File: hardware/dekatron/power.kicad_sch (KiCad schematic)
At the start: 114 parts, among them J101 PWR_IN, J102 NIX_12V, Q101 AOD4185, Q102 AOD5N40, U101 TPS54202, U102 LM66100, U103 LM66100, U104 LM66100, U105 LP2951 (adj. 10 V), U106 LM5156H, U107 TLV3011

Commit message: Tube sheet schematic; kit 15 uH buck inductor
tube.kicad_sch: G+/RTN zener regulator from V_B_BIAS (RTN 51 V sinks the
tube current and holds with zero tube current; G+ = 90 V), MMBTA42 guide
drivers, MMBTA92 index level shifter, 3 x 220k anode string, cathode
links LK6-LK14 and soldered harness landings. Net classes extended to
ANODE (HV) and the bias nets. BOM now covers both sheets (bom.csv).
Buck inductor from the user's kit: 15 uH, 1.31 A, 4 mm pitch.

Co-Authored-By: Claude Opus 5.5 <noreply@anthropic.com>
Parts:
- L101: footprint Inductor_SMD:L_Bourns_SRR1260 -> Inductor_THT:L_Radial_D6.0mm_P4.00mm; MPN SRR1260-150M -> (kit, 6 x 8 mm radial); Manufacturer Bourns -> (none); Rating Isat >= 2.5 A -> Rated 1.31 A; limits the 5 V rail to ~1.3 A
- L102: Rating Rated 0.71 A, DCR 0.35 ohm; confirm lead pitch -> Rated 0.71 A, DCR 0.35 ohm, 4 mm pitch
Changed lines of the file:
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@@
 	  (property "Reference" "L101" (at 398.78 50.34 90) (show_name no) (do_not_autoplace no) (effects (font (size 1.27 1.27))))
 	  (property "Value" "15uH" (at 398.78 57.34 90) (show_name no) (do_not_autoplace no) (effects (font (size 1.27 1.27))))
-	  (property "Footprint" "Inductor_SMD:L_Bourns_SRR1260" (at 398.78 53.34 90) (hide yes) (show_name no) (do_not_autoplace no) (effects (font (size 1.27 1.27)) (justify left)))
+	  (property "Footprint" "Inductor_THT:L_Radial_D6.0mm_P4.00mm" (at 398.78 53.34 90) (hide yes) (show_name no) (do_not_autoplace no) (effects (font (size 1.27 1.27)) (justify left)))
 	  (property "Datasheet" "" (at 398.78 53.34 90) (hide yes) (show_name no) (do_not_autoplace no) (effects (font (size 1.27 1.27)) (justify left)))
 	  (property "Description" "Inductor" (at 398.78 53.34 90) (hide yes) (show_name no) (do_not_autoplace no) (effects (font (size 1.27 1.27)) (justify left)))
 	  (property "Function" "Buck inductor" (at 398.78 53.34 90) (hide yes) (show_name no) (do_not_autoplace no) (effects (font (size 1.27 1.27)) (justify left)))
-	  (property "MPN" "SRR1260-150M" (at 398.78 53.34 90) (hide yes) (show_name no) (do_not_autoplace no) (effects (font (size 1.27 1.27)) (justify left)))
-	  (property "Manufacturer" "Bourns" (at 398.78 53.34 90) (hide yes) (show_name no) (do_not_autoplace no) (effects (font (size 1.27 1.27)) (justify left)))
-	  (property "Rating" "Isat >= 2.5 A" (at 398.78 53.34 90) (hide yes) (show_name no) (do_not_autoplace no) (effects (font (size 1.27 1.27)) (justify left)))
+	  (property "MPN" "(kit, 6 x 8 mm radial)" (at 398.78 53.34 90) (hide yes) (show_name no) (do_not_autoplace no) (effects (font (size 1.27 1.27)) (justify left)))
+	  (property "Rating" "Rated 1.31 A; limits the 5 V rail to ~1.3 A" (at 398.78 53.34 90) (hide yes) (show_name no) (do_not_autoplace no) (effects (font (size 1.27 1.27)) (justify left)))
 	  (pin "1")
 	  (pin "2")
@@
 	  (property "Function" "HV boost inductor" (at 340.36 170.18 90) (hide yes) (show_name no) (do_not_autoplace no) (effects (font (size 1.27 1.27)) (justify left)))
 	  (property "MPN" "(kit, 6 x 8 mm radial)" (at 340.36 170.18 90) (hide yes) (show_name no) (do_not_autoplace no) (effects (font (size 1.27 1.27)) (justify left)))
-	  (property "Rating" "Rated 0.71 A, DCR 0.35 ohm; confirm lead pitch" (at 340.36 170.18 90) (hide yes) (show_name no) (do_not_autoplace no) (effects (font (size 1.27 1.27)) (justify left)))
-	  (pin "1")
-	  (pin "2")
+	  (property "Rating" "Rated 0.71 A, DCR 0.35 ohm, 4 mm pitch" (at 340.36 170.18 90) (hide yes) (show_name no) (do_not_autoplace no) (effects (font (size 1.27 1.27)) (justify left)))
+	  (pin "1")
+	  (pin "2")

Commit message: Schematic review: add V_b overvoltage cutoff; fix bring-up step 2 and SW net class
Netlist checks (117 nets, 91 pin checks, GPIO map, net classes) pass.
Design review found V_b unprotected: with feedback and OVP on HV, an open
tripler part or link LK3 lets V_b run away. A second TLV3011 (2 x 1.0M /
12.4k, ~202 V) is wired-OR on EN/UVLO; simulated with an open tripler
diode, V_b holds at <= 199.3 V. Bring-up step 2 keeps the tripler
connected (LK4 open, HV dummy load); V_b dummy loads removed. Net-class
pattern *SW -> */SW so the buck switch node keeps default clearance.

Co-Authored-By: Claude Opus 5.5 <noreply@anthropic.com>
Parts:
- removed R144: 8.2k, Resistor_SMD:R_1206_3216Metric, symbol Device:R
- added C129: 1nF, Capacitor_SMD:C_1206_3216Metric, symbol Device:C
- added C130: 0.1uF, Capacitor_SMD:C_1206_3216Metric, symbol Device:C
- added U108: TLV3011, Package_TO_SOT_SMD:SOT-23-6, symbol dekatron:TLV3011
- LK3: Function D11 link L3: V_b to the tripler DC column (wire link, desol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 -> D11 link L3: V_b to the tripler DC column (fault isolation;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
- R141: value 8.2k -> 1.0M; Function V_b dummy load 1/4 (bring-up only) -> V_b OVP string 1/2 (<= 100 V per part); now fitted
- R142: value 8.2k -> 1.0M; Function V_b dummy load 2/4 (bring-up only) -> V_b OVP string 2/2; now fitted
- R143: value 8.2k -> 12.4k; Function V_b dummy load 3/4 (bring-up only) -> V_b OVP divider, lower (trip ~202 V); Rating (none) -> 1 %; now fitted
- R145: Function HV dummy load 1/6 (bring-up only) -> HV dummy load 1/6 (bring-up only, LK4 open)
- R146: Function HV dummy load 2/6 (bring-up only) -> HV dummy load 2/6 (bring-up only, LK4 open)
- R147: Function HV dummy load 3/6 (bring-up only) -> HV dummy load 3/6 (bring-up only, LK4 open)
- R148: Function HV dummy load 4/6 (bring-up only) -> HV dummy load 4/6 (bring-up only, LK4 open)
- R149: Function HV dummy load 5/6 (bring-up only) -> HV dummy load 5/6 (bring-up only, LK4 open)
- R150: Function HV dummy load 6/6 (bring-up only) -> HV dummy load 6/6 (bring-up only, LK4 open)
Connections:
- net STR_DV3 is gone; now on net GND: R143.2
- net +5V: now also C130.1, U108.6 (V+)
- net GND: now also C129.2, C130.2, U108.2 (V-)
- net HV_EN_PIN: now also U108.1 (OUT)
- net STR_DV1 renamed STR_VO1
- net STR_DV2 renamed VB_OVP_SENSE
- net VB_OVP_SENSE: now also C129.1, U108.4 (IN-)
- new net VB_OVP_REF: U108.3 (IN+), U108.5 (REF)
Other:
- note added: "HV MONITOR (HV_SENSE, GP28), INDEPENDENT OVP on HV (~548 V) and on V_b (~202 V): both pull EN/UVLO low"
- note removed: "HV MONITOR (HV_SENSE, GP28) and INDEPENDENT OVP (TLV3011, trips at ~548 V, pulls EN/UVLO low)"

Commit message: Tie the dekatron cathodes at the socket; add Phase 1C PCB tooling (WIP)
Cathodes K0, K2-K9 are joined at the socket and return on one RTN wire, as
in the AD01 reference: LK6-LK14 and J203 removed, tube harness is anode
(J201) + G1, G2, K1, RTN (J202, 4 pads). Netlist diff: only the nine
TUBE_Kn nets and the RTN link pins change. ERC 1 (intentional).

Also adds work-in-progress PCB tooling: gen_pcb.py (pcbnew placement,
outline, pours, rules), route_pcb.py (class-aware A* router adapted from
nanovolt-divider), pcb_io.py, and dekatron.kicad_dru with the corrected
HV pair rules (HV to HV/VB/HVSTR 1.5 mm, to bias/logic 3.0 mm). Harness
landings use plain wire pads with cable-tie anchors. The board itself is
not committed yet: placement is being reworked.

Co-Authored-By: Claude Opus 5.5 <noreply@anthropic.com>
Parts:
- J101, J102: footprint Connector_Wire:SolderWire-0.5sqmm_1x02_P4.8mm_D0.9mm_OD2.3mm_Relief -> Connector_Wire:SolderWire-0.5sqmm_1x02_P4.8mm_D0.9mm_OD2.3mm
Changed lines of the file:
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@@
 	  (property "Reference" "J101" (at 33.68 44.72 0) (show_name no) (do_not_autoplace no) (effects (font (size 1.27 1.27)) (justify left)))
 	  (property "Value" "PWR_IN" (at 33.68 47.32 0) (show_name no) (do_not_autoplace no) (effects (font (size 1.27 1.27)) (justify left)))
-	  (property "Footprint" "Connector_Wire:SolderWire-0.5sqmm_1x02_P4.8mm_D0.9mm_OD2.3mm_Relief" (at 30.48 45.72 0) (hide yes) (show_name no) (do_not_autoplace no) (effects (font (size 1.27 1.27)) (justify left)))
+	  (property "Footprint" "Connector_Wire:SolderWire-0.5sqmm_1x02_P4.8mm_D0.9mm_OD2.3mm" (at 30.48 45.72 0) (hide yes) (show_name no) (do_not_autoplace no) (effects (font (size 1.27 1.27)) (justify left)))
 	  (property "Datasheet" "" (at 30.48 45.72 0) (hide yes) (show_name no) (do_not_autoplace no) (effects (font (size 1.27 1.27)) (justify left)))
 	  (property "Description" "Generic connector, single row, 01x02, script generated (kicad-library-utils/schlib/autogen/connector/)" (at 30.48 45.72 0) (hide yes) (show_name no) (do_not_autoplace no) (effects (font (size 1.27 1.27)) (justify left)))
@@
 	  (property "Reference" "J102" (at 285.14 44.72 0) (show_name no) (do_not_autoplace no) (effects (font (size 1.27 1.27)) (justify left)))
 	  (property "Value" "NIX_12V" (at 285.14 47.32 0) (show_name no) (do_not_autoplace no) (effects (font (size 1.27 1.27)) (justify left)))
-	  (property "Footprint" "Connector_Wire:SolderWire-0.5sqmm_1x02_P4.8mm_D0.9mm_OD2.3mm_Relief" (at 281.94 45.72 0) (hide yes) (show_name no) (do_not_autoplace no) (effects (font (size 1.27 1.27)) (justify left)))
+	  (property "Footprint" "Connector_Wire:SolderWire-0.5sqmm_1x02_P4.8mm_D0.9mm_OD2.3mm" (at 281.94 45.72 0) (hide yes) (show_name no) (do_not_autoplace no) (effects (font (size 1.27 1.27)) (justify left)))
 	  (property "Datasheet" "" (at 281.94 45.72 0) (hide yes) (show_name no) (do_not_autoplace no) (effects (font (size 1.27 1.27)) (justify left)))
 	  (property "Description" "Generic connector, single row, 01x02, script generated (kicad-library-utils/schlib/autogen/connector/)" (at 281.94 45.72 0) (hide yes) (show_name no) (do_not_autoplace no) (effects (font (size 1.27 1.27)) (justify left)))

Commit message: Redraw the dekatron schematics as wired, readable sheets
Each block is now drawn with real wires, power/GND symbols and junctions
instead of per-pin label stubs. Net names used by the PCB scripts and net
classes are kept as local labels; inter-sheet nets stay global labels.
Netlist pin partition verified identical to the previous version; ERC
unchanged (1 intentional LP2951/LM5156 power-output violation).

Co-Authored-By: Claude Opus 5.5 <noreply@anthropic.com>
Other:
- note added: "10 V GATE DRIVE"
- note added: "12 V INPUT (D4)"
- note added: "5 V BUCK"
- note added: "Bleeder, feedback, monitor and OVP strings, each part <= 150 V; always connected"
- note added: "Every capacitor and diode sees <= V_b; 47 ohm pump surge resistor; LK3 isolates the DC column for fault finding (never powered open)"
- note added: "Fuse, reverse-polarity P-MOSFET (gate clamped by D101), TVS, bulk; fused branch to the Nixie module"
- note added: "HV BOOST (D2, Phase 1B)"
- note added: "HV STRINGS (D2, D3, D12)"
- note added: "IDEAL DIODES (D6)"
- note added: "LM5156H, ~150 kHz DCM, 10 V gate drive, feedback from HV (tripler sheet area), CS filter against the pump surge; kit 100 uH inductor"
- note added: "LP2951 feeds LM5156 BIAS = VCC (2.97-16 V mode); 143k / 20.0k -> 10.07 V"
- note added: "One LM66100 per external 5 V feed; CE grounded = always on"
- note added: "TPS54202, TI reference design (SLVSD26C Fig. 7-1); 100k / 13.7k -> 4.95 V; UVLO 511k / 105k"
- note added: "TRIPLER (series-stack Cockcroft-Walton)"
- note removed: "10 V GATE DRIVE: LP2951 feeds LM5156 BIAS = VCC (2.97-16 V mode); 143k/20.0k -> 10.07 V"
- note removed: "12 V INPUT (D4): fuse, reverse-polarity P-MOSFET, TVS, bulk; Nixie module branch"
- note removed: "5 V BUCK: TPS54202, TI reference design (SLVSD26C Fig. 7-1); 100k/13.7k -> 4.95 V"
- note removed: "HV BOOST (D2, Phase 1B): LM5156H, ~150 kHz DCM, feedback from HV, CS filter, 10 V drive; kit 100 uH inductor"
- note removed: "HV MONITOR (HV_SENSE, GP28), INDEPENDENT OVP on HV (~548 V) and on V_b (~202 V): both pull EN/UVLO low"
- note removed: "IDEAL DIODES (D6): one LM66100 per external 5 V feed; CE grounded = always on"
- note removed: "TRIPLER (series-stack CW): every capacitor and diode sees <= V_b; 47 ohm pump surge resistor"
- moved on the sheet: F101, R134, R135

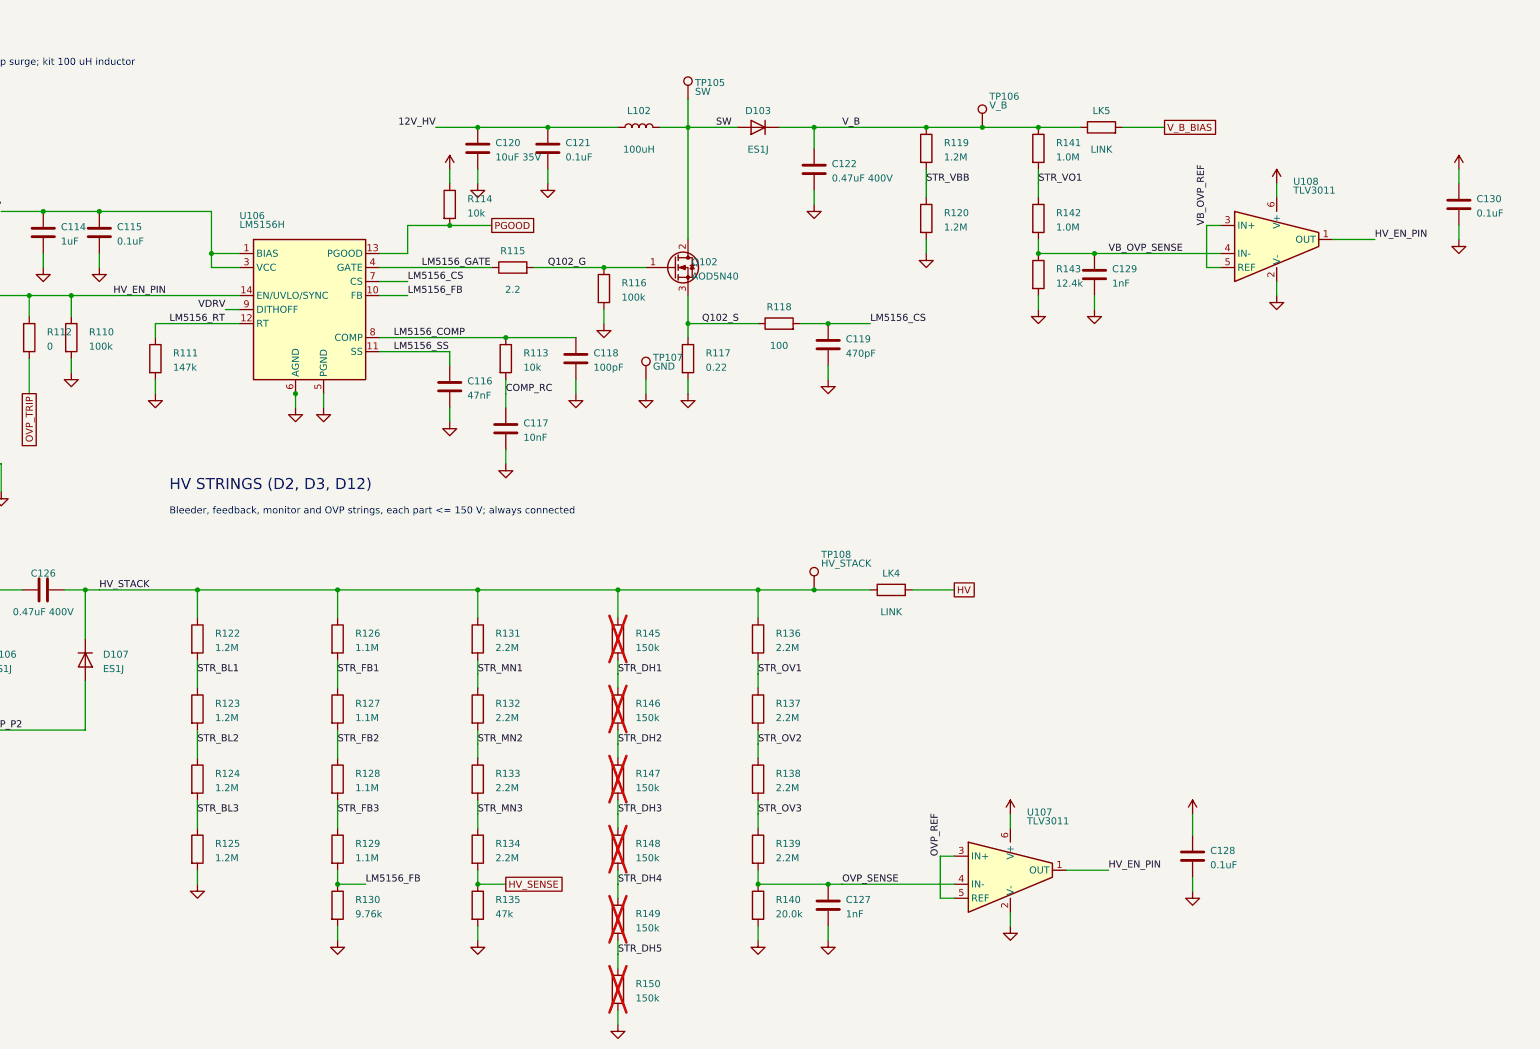
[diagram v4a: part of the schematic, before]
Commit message: Replace 1206 HV resistor strings with single leaded HVR25/HVR37 parts
- Drop the dedicated HV bleeder; the feedback divider (HVR25 4.75M/10.5k,
  453.4 V) and a shared monitor/OVP divider (HVR25 4.64M/14.0k/10.5k,
  OVP 551.8 V, HV_SENSE = HV/190.4) discharge HV: <50 V in 1.94 s,
  3.9 s with one divider open (hv_discharge.cir).
- Dummy load: one DNP HVR37 910k. V_b bleeder/OVP, RTN_SENSE, index
  divider: single HVR25. Anode: 2 x HVR37 332k. G+/RTN feed: MRS25 40.2k.
- C304 (HV_SENSE) 100 nF -> 10 nF: on a feedback-open runaway the shared
  OVP tap lagged HV by 15.8 V with 100 nF (fault_fbopen.cir).
- BOM 180 -> 155 parts; ERC unchanged.

Co-Authored-By: Claude Opus 5.5 <noreply@anthropic.com>
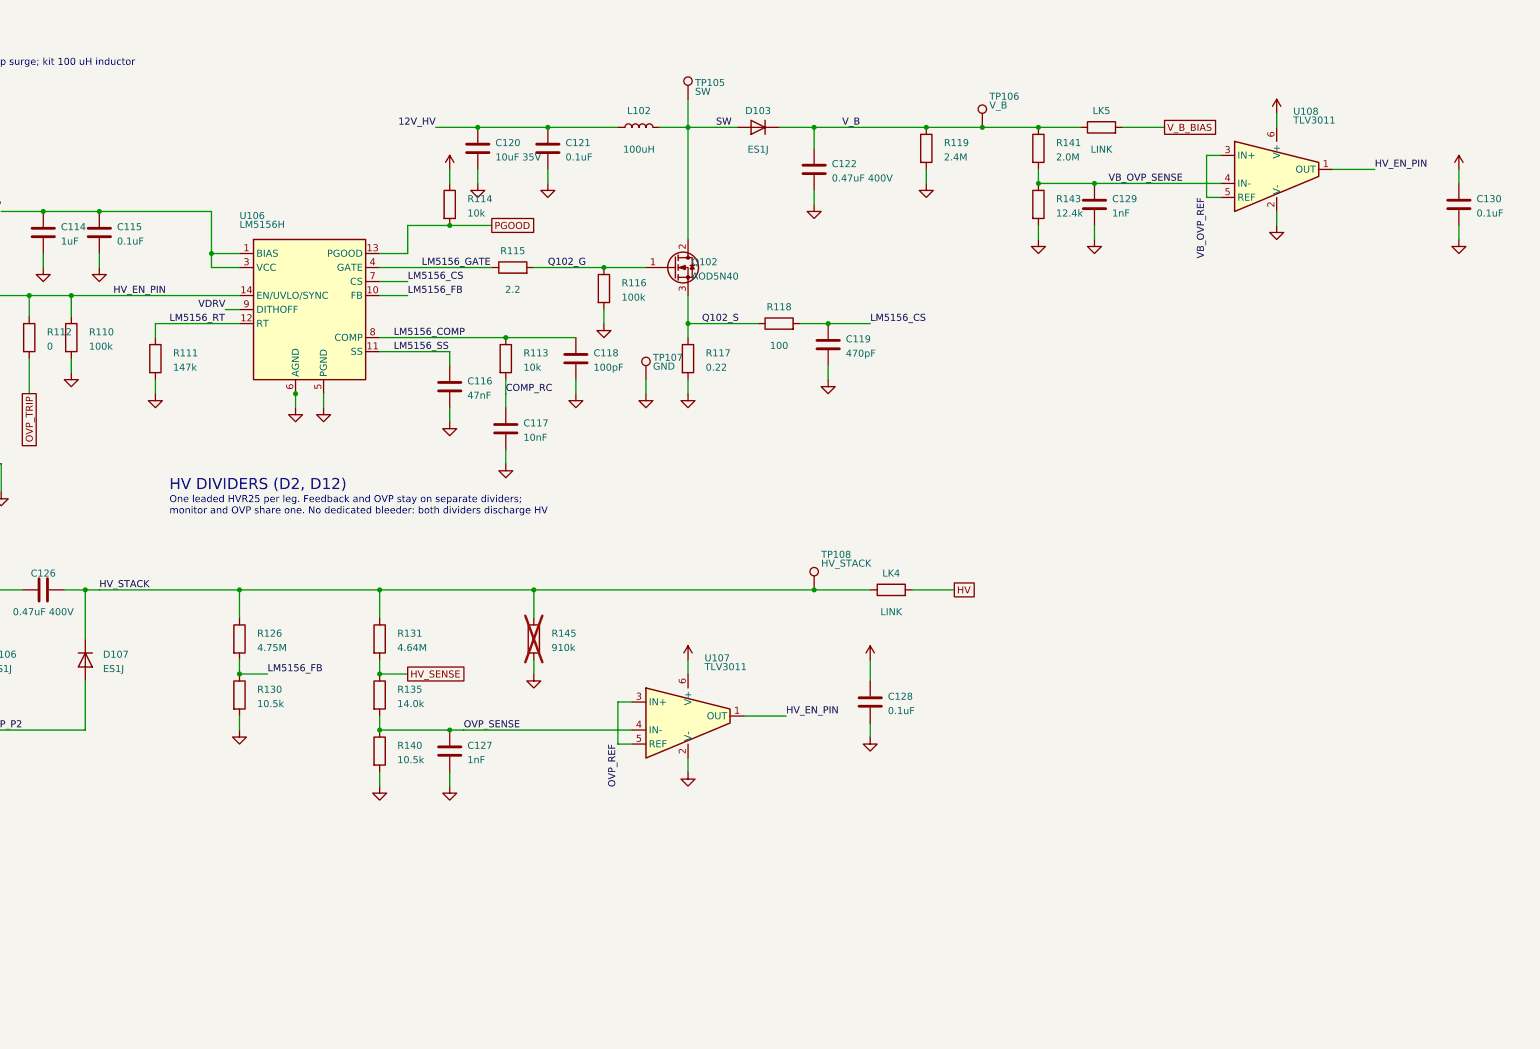
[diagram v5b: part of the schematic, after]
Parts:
- removed R120, R122, R123, R124, R125: 1.2M, Resistor_SMD:R_1206_3216Metric, symbol Device:R
- removed R127, R128, R129: 1.1M, Resistor_SMD:R_1206_3216Metric, symbol Device:R
- removed R132, R133, R134, R136, R137, R138, R139: 2.2M, Resistor_SMD:R_1206_3216Metric, symbol Device:R
- removed R142: 1.0M, Resistor_SMD:R_1206_3216Metric, symbol Device:R
- removed R146, R147, R148, R149, R150: 150k, Resistor_SMD:R_1206_3216Metric, symbol Device:R
- R119: value 1.2M -> 2.4M; footprint Resistor_SMD:R_1206_3216Metric -> Resistor_THT:R_Axial_DIN0207_L6.3mm_D2.5mm_P10.16mm_Horizontal; Function V_b bleeder 1/2 -> V_b bleeder (V_b's own discharge path with L3 open); MPN (none) -> HVR2500002404FR500; Manufacturer (none) -> Vishay; Rating (none) -> HVR25: 0.25 W, 1600 V DC, 1 %, 200 ppm/K
- R126: value 1.1M -> 4.75M; footprint Resistor_SMD:R_1206_3216Metric -> Resistor_THT:R_Axial_DIN0207_L6.3mm_D2.5mm_P10.16mm_Horizontal; Function HV feedback string 1/4 -> HV feedback divider, upper; MPN (none) -> HVR2500004754FR500; Manufacturer (none) -> Vishay; Rating (none) -> HVR25: 0.25 W, 1600 V DC, 1 %, 200 ppm/K
- R130: value 9.76k -> 10.5k; Function HV feedback, lower (451.8 V; 8.87k for 500 V) -> HV feedback, lower (453.4 V; 9.53k for 500 V)
- R131: value 2.2M -> 4.64M; footprint Resistor_SMD:R_1206_3216Metric -> Resistor_THT:R_Axial_DIN0207_L6.3mm_D2.5mm_P10.16mm_Horizontal; Function HV monitor string 1/4 -> HV monitor / OVP divider, upper; MPN (none) -> HVR2500004644FR500; Manufacturer (none) -> Vishay; Rating (none) -> HVR25: 0.25 W, 1600 V DC, 1 %, 200 ppm/K
- R135: value 47k -> 14.0k; Function HV monitor, lower (2.39 V at 450 V) -> HV monitor / OVP divider, middle (HV_SENSE 2.36 V at 450 V)
- R140: value 20.0k -> 10.5k; Function OVP divider, lower (trip ~548 V) -> HV monitor / OVP divider, lower (OVP trip 551.8 V)
- R141: value 1.0M -> 2.0M; footprint Resistor_SMD:R_1206_3216Metric -> Resistor_THT:R_Axial_DIN0207_L6.3mm_D2.5mm_P10.16mm_Horizontal; Function V_b OVP string 1/2 (<= 100 V per part) -> V_b OVP divider, upper; MPN (none) -> HVR2500002004FR500; Manufacturer (none) -> Vishay; Rating (none) -> HVR25: 0.25 W, 1600 V DC, 1 %, 200 ppm/K
- R145: value 150k -> 910k; footprint Resistor_SMD:R_1206_3216Metric -> Resistor_THT:R_Axial_DIN0411_L9.9mm_D3.6mm_P15.24mm_Horizontal; Function HV dummy load 1/6 (bring-up only, LK4 open) -> HV dummy load (bring-up only, LK4 open); MPN (none) -> HVR3700009103FR500; Manufacturer (none) -> Vishay; Rating (none) -> HVR37: 0.5 W, 3500 V DC, 1 %, 200 ppm/K
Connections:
- net STR_DH1 is gone; now on net GND: R145.2
- net STR_FB1 is gone; now on net LM5156_FB: R126.2
- net STR_MN1 is gone; now on net HV_SENSE: R131.2
- net STR_VBB is gone; now on net GND: R119.2
- net STR_VO1 is gone; now on net VB_OVP_SENSE: R141.2
- net GND: no longer R135.2
- net OVP_SENSE: now also R135.2
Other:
- note added: "HV DIVIDERS (D2, D12)"
- note added: "One leaded HVR25 per leg. Feedback and OVP stay on separate dividers; monitor and OVP share one. No dedicated bleeder: both dividers discharge HV"
- note removed: "Bleeder, feedback, monitor and OVP strings, each part <= 150 V; always connected"
- note removed: "HV STRINGS (D2, D3, D12)"
